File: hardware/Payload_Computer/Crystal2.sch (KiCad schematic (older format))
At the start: 1 part, among them Y2 Crystal_GND24

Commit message: Minor Library Changes
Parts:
- Y2: symbol Payload_Computer-rescue:Crystal_GND24-Symbols -> Symbols:Crystal_GND24
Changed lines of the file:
@@
 $Descr A4 11693 8268
 encoding utf-8
-Sheet 4 21
+Sheet 4 24
 Title ""
 Date ""
@@
 $EndDescr
 $Comp
-L Payload_Computer-rescue:Crystal_GND24-Symbols Y2
+L Symbols:Crystal_GND24 Y2
 U 1 1 5F851061
 P 6050 3900

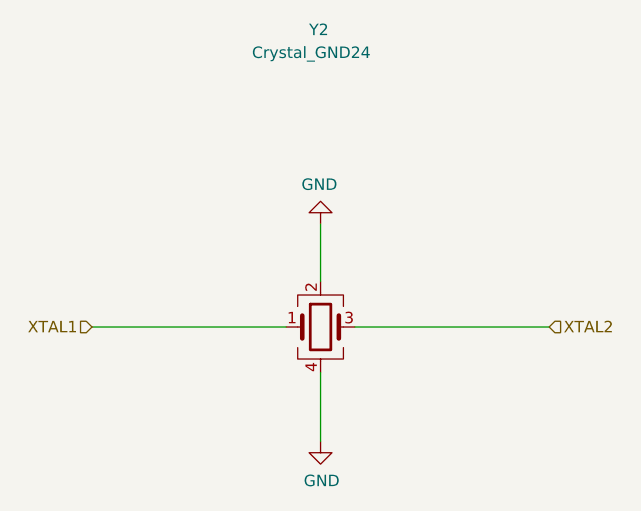
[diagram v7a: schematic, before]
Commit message: Added last footprints and started routing
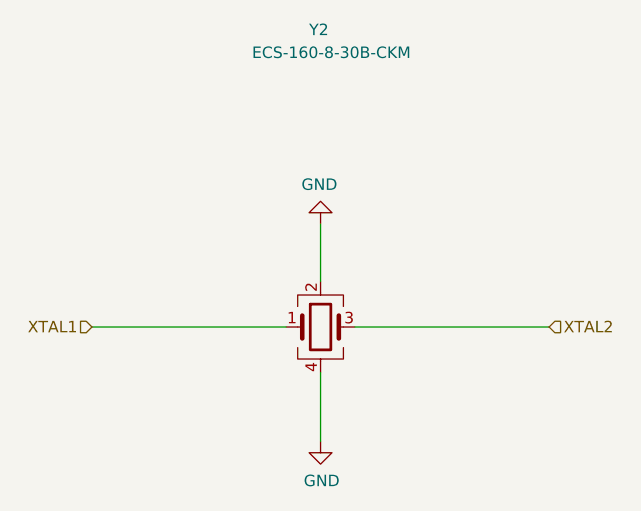
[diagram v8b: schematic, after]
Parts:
- Y2: value Crystal_GND24 -> ECS-160-8-30B-CKM; footprint (none) -> LED:16Mhz
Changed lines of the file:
@@
 P 6050 3900
 F 0 "Y2" H 6000 5200 50  0000 L CNN
-F 1 "Crystal_GND24" H 5750 5100 50  0000 L CNN
-F 2 "" H 6050 3900 50  0001 C CNN
+F 1 "ECS-160-8-30B-CKM" H 5750 5100 50  0000 L CNN
+F 2 "LED:16Mhz" H 6050 3900 50  0001 C CNN
 F 3 "~" H 6050 3900 50  0001 C CNN
 	1    6050 3900
